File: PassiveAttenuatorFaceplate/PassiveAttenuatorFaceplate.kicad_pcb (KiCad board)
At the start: 2 copper layers, 15 x 128.5 mm, 8 parts

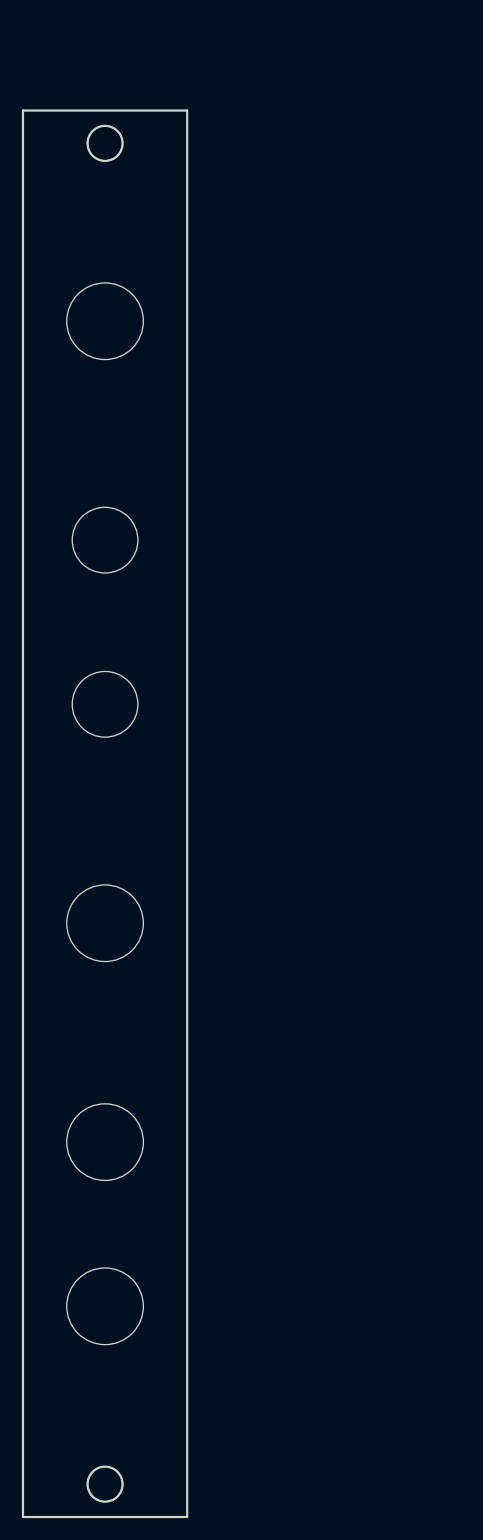
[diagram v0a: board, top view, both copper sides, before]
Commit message: Finish faceplate, add gerbers
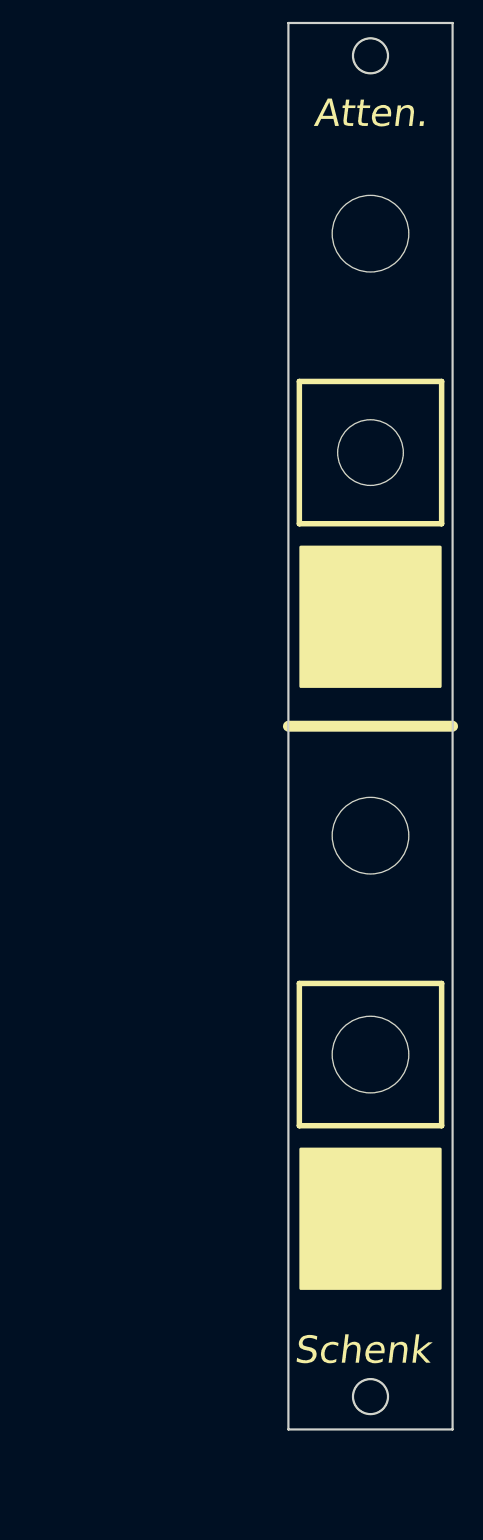
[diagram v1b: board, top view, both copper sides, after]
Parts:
- removed the REF** at (125.8, 140.5)
- removed the REF** at (125.8, 125.5)
- removed the REF** at (125.8, 105.5)
- removed the REF** at (125.8, 85.5)
- removed the REF** at (125.8, 70.5)
- removed the REF** at (125.8, 50.5)
- removed the REF** at (125.8, 34.2)
- removed the REF** at (125.8, 156.8)
- added REF**: MountingHole, Mounting_Holes:MountingHole_3.2mm_M3, F.Cu at (150.0, 132.5)
- added REF**: MountingHole, Mounting_Holes:MountingHole_3.2mm_M3, F.Cu at (150.0, 117.5)
- added REF**: MountingHole, Mounting_Holes:MountingHole_3.2mm_M3, F.Cu at (150.0, 97.5)
- added REF**: MountingHole, Mounting_Holes:MountingHole_3.2mm_M3, F.Cu at (150.0, 77.5)
- added REF**: MountingHole, Mounting_Holes:MountingHole_3.2mm_M3, F.Cu at (150.0, 62.5)
- added REF**: MountingHole, Mounting_Holes:MountingHole_3.2mm_M3, F.Cu at (150.0, 42.5)
- added REF**: MountingHole, Mounting_Holes:MountingHole_3.2mm_M3, F.Cu at (150.0, 26.2)
- added REF**: MountingHole, Mounting_Holes:MountingHole_3.2mm_M3, F.Cu at (150.0, 148.8)
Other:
- board text added: "Atten."
- board text added: "Schenk"
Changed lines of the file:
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@@
   (general
     (thickness 1.6)
-    (drawings 6)
+    (drawings 17)
     (tracks 0)
     (zones 0)
@@
     (mod_text_size 1 1)
     (mod_text_width 0.15)
-    (pad_size 7 7)
-    (pad_drill 7)
+    (pad_size 6 6)
+    (pad_drill 6)
     (pad_to_mask_clearance 0.051)
     (solder_mask_min_width 0.25)
@@
       (outputformat 1)
       (mirror false)
-      (drillshape 1)
+      (drillshape 0)
       (scaleselection 1)
-      (outputdirectory ""))
+      (outputdirectory "Gerbers/"))
   )
   (net 0 "")
@@
   )
   (module Mounting_Holes:MountingHole_3.2mm_M3 (layer F.Cu)
-    (at 125.75 140.499999 180)
-    (descr "Mounting Hole 3.2mm, no annular, M3")
-    (tags "mounting hole 3.2mm no annular m3")
-    (attr virtual)
-    (fp_text reference REF** (at 0 -4.2) (layer F.SilkS) hide
-      (effects (font (size 1 1) (thickness 0.15)))
-    )
-    (fp_text value MountingHole (at 0 4.2) (layer F.Fab) hide
-      (effects (font (size 1 1) (thickness 0.15)))
-    )
-    (pad "" np_thru_hole circle (at 0 0 180) (size 7 7) (drill 7) (layers *.Cu *.Mask))
-  )
-  (module Mounting_Holes:MountingHole_3.2mm_M3 (layer F.Cu)
-    (at 125.75 125.499999 180)
-    (descr "Mounting Hole 3.2mm, no annular, M3")
-    (tags "mounting hole 3.2mm no annular m3")
-    (attr virtual)
-    (fp_text reference REF** (at 0 -4.2) (layer F.SilkS) hide
-      (effects (font (size 1 1) (thickness 0.15)))
-    )
-    (fp_text value MountingHole (at 0 4.2) (layer F.Fab) hide
-      (effects (font (size 1 1) (thickness 0.15)))
-    )
-    (pad "" np_thru_hole circle (at 0 0 180) (size 7 7) (drill 7) (layers *.Cu *.Mask))
-  )
-  (module Mounting_Holes:MountingHole_3.2mm_M3 (layer F.Cu)
-    (at 125.75 105.499999 180)
-    (descr "Mounting Hole 3.2mm, no annular, M3")
-    (tags "mounting hole 3.2mm no annular m3")
-    (attr virtual)
-    (fp_text reference REF** (at 0 -4.2) (layer F.SilkS) hide
-      (effects (font (size 1 1) (thickness 0.15)))
-    )
-    (fp_text value MountingHole (at 0 4.2) (layer F.Fab) hide
-      (effects (font (size 1 1) (thickness 0.15)))
-    )
-    (pad "" np_thru_hole circle (at 0 0 180) (size 7 7) (drill 7) (layers *.Cu *.Mask))
-  )
-  (module Mounting_Holes:MountingHole_3.2mm_M3 (layer F.Cu)
-    (at 125.75 85.499999 180)
+    (at 150 132.499999 180)
+    (descr "Mounting Hole 3.2mm, no annular, M3")
+    (tags "mounting hole 3.2mm no annular m3")
+    (attr virtual)
+    (fp_text reference REF** (at 0 -4.2) (layer F.SilkS) hide
+      (effects (font (size 1 1) (thickness 0.15)))
+    )
+    (fp_text value MountingHole (at 0 4.2) (layer F.Fab) hide
+      (effects (font (size 1 1) (thickness 0.15)))
+    )
+    (pad "" np_thru_hole circle (at 0 0 180) (size 7 7) (drill 7) (layers *.Cu *.Mask))
+  )
+  (module Mounting_Holes:MountingHole_3.2mm_M3 (layer F.Cu)
+    (at 150 117.499999 180)
+    (descr "Mounting Hole 3.2mm, no annular, M3")
+    (tags "mounting hole 3.2mm no annular m3")
+    (attr virtual)
+    (fp_text reference REF** (at 0 -4.2) (layer F.SilkS) hide
+      (effects (font (size 1 1) (thickness 0.15)))
+    )
+    (fp_text value MountingHole (at 0 4.2) (layer F.Fab) hide
+      (effects (font (size 1 1) (thickness 0.15)))
+    )
+    (pad "" np_thru_hole circle (at 0 0 180) (size 7 7) (drill 7) (layers *.Cu *.Mask))
+  )
+  (module Mounting_Holes:MountingHole_3.2mm_M3 (layer F.Cu)
+    (at 150 97.499999 180)
+    (descr "Mounting Hole 3.2mm, no annular, M3")
+    (tags "mounting hole 3.2mm no annular m3")
+    (attr virtual)
+    (fp_text reference REF** (at 0 -4.2) (layer F.SilkS) hide
+      (effects (font (size 1 1) (thickness 0.15)))
+    )
+    (fp_text value MountingHole (at 0 4.2) (layer F.Fab) hide
+      (effects (font (size 1 1) (thickness 0.15)))
+    )
+    (pad "" np_thru_hole circle (at 0 0 180) (size 7 7) (drill 7) (layers *.Cu *.Mask))
+  )
+  (module Mounting_Holes:MountingHole_3.2mm_M3 (layer F.Cu)
+    (at 150 77.499999 180)
     (descr "Mounting Hole 3.2mm, no annular, M3")
     (tags "mounting hole 3.2mm no annular m3")
@@
   )
   (module Mounting_Holes:MountingHole_3.2mm_M3 (layer F.Cu)
-    (at 125.75 70.499999 180)
+    (at 150 62.499999 180)
     (descr "Mounting Hole 3.2mm, no annular, M3")
     (tags "mounting hole 3.2mm no annular m3")
@@
   )
   (module Mounting_Holes:MountingHole_3.2mm_M3 (layer F.Cu)
-    (at 125.75 50.499999 180)
-    (descr "Mounting Hole 3.2mm, no annular, M3")
-    (tags "mounting hole 3.2mm no annular m3")
-    (attr virtual)
-    (fp_text reference REF** (at 0 -4.2) (layer F.SilkS) hide
-      (effects (font (size 1 1) (thickness 0.15)))
-    )
-    (fp_text value MountingHole (at 0 4.2) (layer F.Fab) hide
-      (effects (font (size 1 1) (thickness 0.15)))
-    )
-    (pad "" np_thru_hole circle (at 0 0 180) (size 7 7) (drill 7) (layers *.Cu *.Mask))
-  )
-  (module Mounting_Holes:MountingHole_3.2mm_M3 (layer F.Cu)
-    (at 125.75 34.249999 180)
+    (at 150 42.499999 180)
+    (descr "Mounting Hole 3.2mm, no annular, M3")
+    (tags "mounting hole 3.2mm no annular m3")
+    (attr virtual)
+    (fp_text reference REF** (at 0 -4.2) (layer F.SilkS) hide
+      (effects (font (size 1 1) (thickness 0.15)))
+    )
+    (fp_text value MountingHole (at 0 4.2) (layer F.Fab) hide
+      (effects (font (size 1 1) (thickness 0.15)))
+    )
+    (pad "" np_thru_hole circle (at 0 0 180) (size 7 7) (drill 7) (layers *.Cu *.Mask))
+  )
+  (module Mounting_Holes:MountingHole_3.2mm_M3 (layer F.Cu)
+    (at 150 26.249999 180)
     (descr "Mounting Hole 3.2mm, no annular, M3")
     (tags "mounting hole 3.2mm no annular m3")
@@
   )
   (module Mounting_Holes:MountingHole_3.2mm_M3 (layer F.Cu)
-    (at 125.75 156.75 180)
+    (at 150 148.75 180)
     (descr "Mounting Hole 3.2mm, no annular, M3")
     (tags "mounting hole 3.2mm no annular m3")
@@
     (pad "" np_thru_hole circle (at 0 0 180) (size 3.2 3.2) (drill 3.2) (layers *.Cu *.Mask))
   )
-  (gr_line (start 133.25 31.250001) (end 133.25 159.750001) (layer Edge.Cuts) (width 0.2))
-  (gr_circle (center 125.75 34.250001) (end 124.15 34.250001) (layer Edge.Cuts) (width 0.2))
-  (gr_line (start 118.25 31.250001) (end 133.25 31.250001) (layer Edge.Cuts) (width 0.2))
-  (gr_line (start 118.25 159.750001) (end 118.25 31.250001) (layer Edge.Cuts) (width 0.2))
-  (gr_line (start 133.25 159.750001) (end 118.25 159.750001) (layer Edge.Cuts) (width 0.2))
-  (gr_circle (center 125.75 156.750001) (end 124.15 156.750001) (layer Edge.Cuts) (width 0.2))
+  (gr_line (start 142.5 87.5) (end 157.5 87.5) (layer F.SilkS) (width 1))
+  (gr_line (start 143.5 111) (end 143.5 124) (layer F.SilkS) (width 0.5))
+  (gr_line (start 156.5 111) (end 143.5 111) (layer F.SilkS) (width 0.5))
+  (gr_line (start 156.5 124) (end 156.5 111) (layer F.SilkS) (width 0.5))
+  (gr_line (start 143.5 124) (end 156.5 124) (layer F.SilkS) (width 0.5))
+  (gr_line (start 143.5 56) (end 143.5 69) (layer F.SilkS) (width 0.5))
+  (gr_line (start 156.5 56) (end 143.5 56) (layer F.SilkS) (width 0.5))
+  (gr_line (start 156.5 69) (end 156.5 56) (layer F.SilkS) (width 0.5))
+  (gr_line (start 143.5 69) (end 156.5 69) (layer F.SilkS) (width 0.5))
+  (gr_text Atten. (at 150 31.500001) (layer F.SilkS)
+    (effects (font (size 2.5 2.5) (thickness 0.4) italic))
+  )
+  (gr_text Schenk (at 143 144.5) (layer F.SilkS)
+    (effects (font (size 2.5 2.5) (thickness 0.4) italic) (justify left))
+  )
+  (gr_line (start 157.5 23.250001) (end 157.5 151.750001) (layer Edge.Cuts) (width 0.2))
+  (gr_circle (center 150 26.250001) (end 148.4 26.250001) (layer Edge.Cuts) (width 0.2))
+  (gr_line (start 142.5 23.250001) (end 157.5 23.250001) (layer Edge.Cuts) (width 0.2))
+  (gr_line (start 142.5 151.750001) (end 142.5 23.250001) (layer Edge.Cuts) (width 0.2))
+  (gr_line (start 157.5 151.750001) (end 142.5 151.750001) (layer Edge.Cuts) (width 0.2))
+  (gr_circle (center 150 148.750001) (end 148.4 148.750001) (layer Edge.Cuts) (width 0.2))
+  (zone (net 0) (net_name "") (layer F.SilkS) (hatch edge 0.508)
+    (connect_pads (clearance 0.508))
+    (min_thickness 0.254)
+    (fill yes (arc_segments 32) (thermal_gap 0.508) (thermal_bridge_width 0.508))
+    (polygon
+      (pts
+        (xy 143.5 126) (xy 156.5 126) (xy 156.5 139) (xy 143.5 139)
+      )
+    )
+  )
+  (zone (net 0) (net_name "") (layer F.SilkS) (hatch edge 0.508)
+    (connect_pads (clearance 0.508))
+    (min_thickness 0.254)
+    (fill yes (arc_segments 32) (thermal_gap 0.508) (thermal_bridge_width 0.508))
+    (polygon
+      (pts
+        (xy 143.5 71) (xy 156.5 71) (xy 156.5 84) (xy 143.5 84)
+      )
+    )
+  )
 )
